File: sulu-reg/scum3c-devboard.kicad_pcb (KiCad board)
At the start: 2 copper layers, 41.7 x 36.1 mm, 55 parts, among them J1 Conn_02x11_Odd_Even, J10 through_hole, J11 through_hole, J12 through_hole, J13 through_hole, J14 through_hole, J15 through_hole, J16 through_hole, J17 through_hole, J18 through_hole, J19 through_hole, J2 Conn_02x10_Odd_Even, J20 through_hole, J21 through_hole, J3 Conn_02x05_Odd_Even, J4 73391-0060, J5 through_hole, J6 through_hole, J7 through_hole, J8 through_hole, J9 through_hole, U1 scum3, U2 S-85S1AB18-I6T1U, U3 S-85S1AB11-I6T1U, U9AB1 ICM-20948

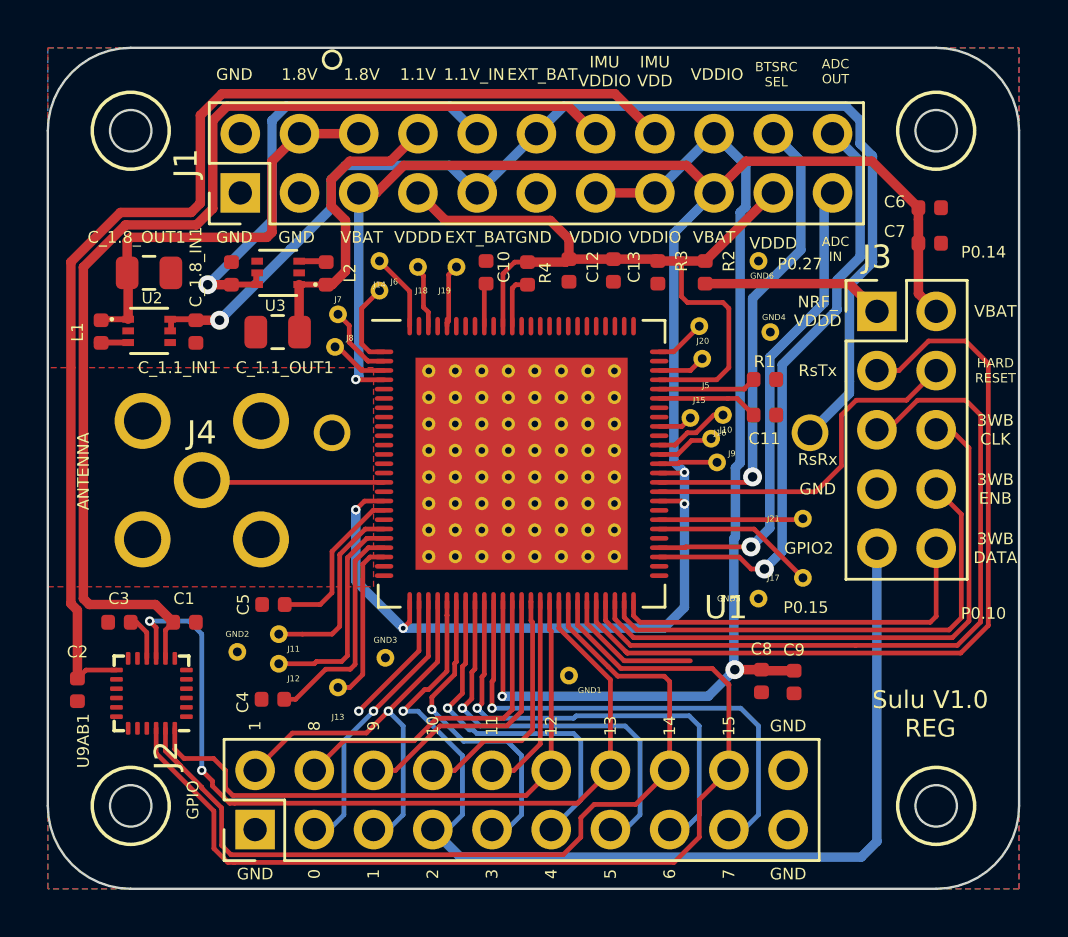
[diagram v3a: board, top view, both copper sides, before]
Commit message: added gnd connections to antenna
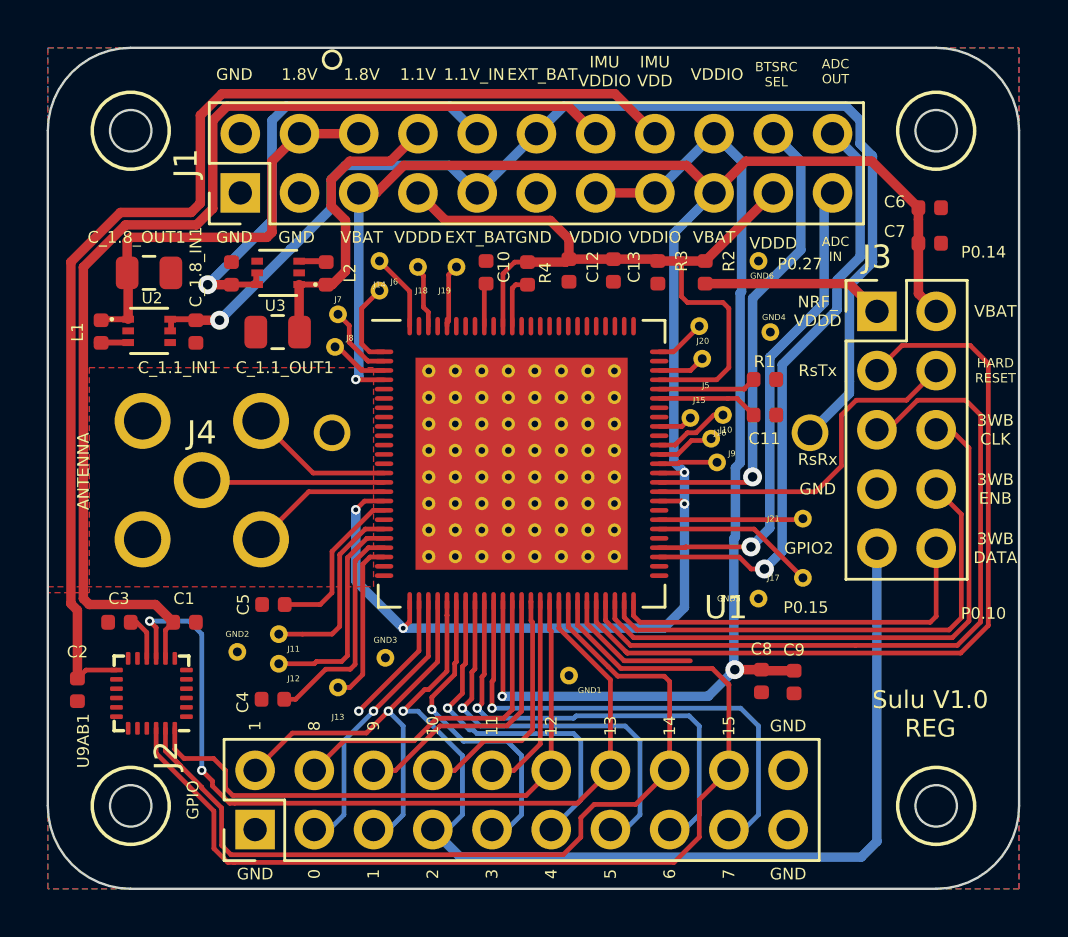
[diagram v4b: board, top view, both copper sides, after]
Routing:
- net GND: track 11.8 -> 24.2 mm
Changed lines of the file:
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@@
     (thickness 1.6)
     (drawings 783)
-    (tracks 508)
+    (tracks 511)
     (zones 0)
     (modules 55)
@@
   (layers
     (0 F.Cu mixed)
-    (31 B.Cu mixed hide)
+    (31 B.Cu mixed)
     (32 B.Adhes user)
     (33 F.Adhes user)
@@
     (pad_to_mask_clearance 0)
     (aux_axis_origin 0 0)
-    (grid_origin 121.285 75.565)
     (visible_elements 7FFFFFFF)
     (pcbplotparams
@@
   (segment (start 121.965 96.255) (end 121.965 98.38) (width 0.2032) (layer F.Cu) (net 1) (status 10))
   (segment (start 121.965 98.38) (end 119.38 100.965) (width 0.2032) (layer F.Cu) (net 1))
+  (segment (start 117.425 90.755) (end 115.189 88.519) (width 0.2032) (layer F.Cu) (net 1))
+  (segment (start 120.465 90.755) (end 117.425 90.755) (width 0.2032) (layer F.Cu) (net 1))
+  (segment (start 117.233 91.555) (end 120.465 91.555) (width 0.2032) (layer F.Cu) (net 1))
+  (segment (start 115.189 93.599) (end 117.233 91.555) (width 0.2032) (layer F.Cu) (net 1))
   (via (at 133.35 92.075) (size 0.4064) (drill 0.2032) (layers F.Cu B.Cu) (net 2))
   (segment (start 132.265 91.955) (end 133.23 91.955) (width 0.2032) (layer F.Cu) (net 2) (status 10))
@@
   (segment (start 134.366 100.33) (end 135.509 99.187) (width 0.4064) (layer B.Cu) (net 4))
   (segment (start 125.5332 100.33) (end 134.366 100.33) (width 0.4064) (layer B.Cu) (net 4))
-  (segment (start 135.979799 77.559799) (end 134.62 76.2) (width 0.4064) (layer B.Cu) (net 4))
-  (segment (start 135.979799 79.337799) (end 135.979799 77.559799) (width 0.4064) (layer B.Cu) (net 4))
-  (segment (start 135.73758 79.580018) (end 135.979799 79.337799) (width 0.4064) (layer B.Cu) (net 4))
-  (segment (start 135.73758 90.32242) (end 135.73758 79.580018) (width 0.4064) (layer B.Cu) (net 4))
   (segment (start 135.509 99.187) (end 135.466386 99.144386) (width 0.4064) (layer B.Cu) (net 4))
   (segment (start 135.534389 93.499441) (end 135.534389 90.525611) (width 0.4064) (layer B.Cu) (net 4))
@@
   (segment (start 135.466386 93.567444) (end 135.534389 93.499441) (width 0.4064) (layer B.Cu) (net 4))
   (segment (start 135.534389 90.525611) (end 135.73758 90.32242) (width 0.4064) (layer B.Cu) (net 4))
+  (segment (start 135.73758 83.038467) (end 135.73758 90.32242) (width 0.4064) (layer B.Cu) (net 4))
+  (segment (start 135.800201 82.975846) (end 135.73758 83.038467) (width 0.4064) (layer B.Cu) (net 4))
+  (segment (start 135.800201 77.380201) (end 135.800201 82.975846) (width 0.4064) (layer B.Cu) (net 4))
+  (segment (start 134.62 76.2) (end 135.800201 77.380201) (width 0.4064) (layer B.Cu) (net 4))
   (segment (start 135.607 87.555) (end 136.317 88.265) (width 0.2032) (layer F.Cu) (net 5))
   (segment (start 135.203 87.555) (end 135.607 87.555) (width 0.2032) (layer F.Cu) (net 5))
@@
   (segment (start 130.828526 98.406474) (end 130.897893 98.47584) (width 0.2032) (layer F.Cu) (net 18))
   (segment (start 129.565 97.142947) (end 130.828526 98.406474) (width 0.2032) (layer F.Cu) (net 18))
-  (segment (start 142.54867 86.36) (end 141.605 86.36) (width 0.2032) (layer F.Cu) (net 18))
-  (segment (start 143.81867 85.09) (end 142.54867 86.36) (width 0.2032) (layer F.Cu) (net 18))
-  (segment (start 145.415 85.09) (end 143.81867 85.09) (width 0.2032) (layer F.Cu) (net 18))
   (segment (start 130.828526 98.406474) (end 130.897892 98.47584) (width 0.2032) (layer F.Cu) (net 18))
-  (segment (start 146.38021 86.05521) (end 145.415 85.09) (width 0.2032) (layer F.Cu) (net 18))
   (segment (start 130.897892 98.47584) (end 145.196146 98.47584) (width 0.2032) (layer F.Cu) (net 18))
   (segment (start 145.196146 98.47584) (end 146.38021 97.291777) (width 0.2032) (layer F.Cu) (net 18))
   (segment (start 146.38021 97.291777) (end 146.38021 86.05521) (width 0.2032) (layer F.Cu) (net 18))
+  (segment (start 145.606399 85.281399) (end 146.38021 86.05521) (width 0.2032) (layer F.Cu) (net 18))
+  (segment (start 142.683601 85.281399) (end 145.606399 85.281399) (width 0.2032) (layer F.Cu) (net 18))
+  (segment (start 141.605 86.36) (end 142.683601 85.281399) (width 0.2032) (layer F.Cu) (net 18))
   (segment (start 142.071986 88.9) (end 141.605 88.9) (width 0.2032) (layer F.Cu) (net 19) (status 30))
   (segment (start 143.341986 87.63) (end 142.071986 88.9) (width 0.2032) (layer F.Cu) (net 19) (status 20))
@@
       (pts
         (xy 147.701 108.585) (xy 106.045 108.585) (xy 106.045 95.631) (xy 120.015 95.631) (xy 120.015 86.233)
-        (xy 106.045 86.233) (xy 106.045 72.517) (xy 147.701 72.517)
+        (xy 107.823 86.233) (xy 107.823 95.885) (xy 106.045 95.885) (xy 106.045 72.517) (xy 147.701 72.517)
       )
     )

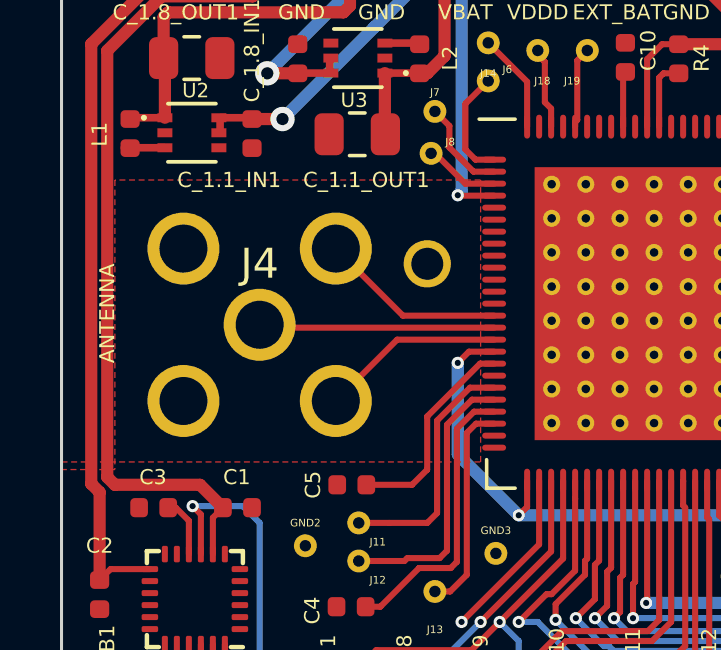
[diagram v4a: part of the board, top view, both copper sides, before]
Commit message: put ground on west of antenna
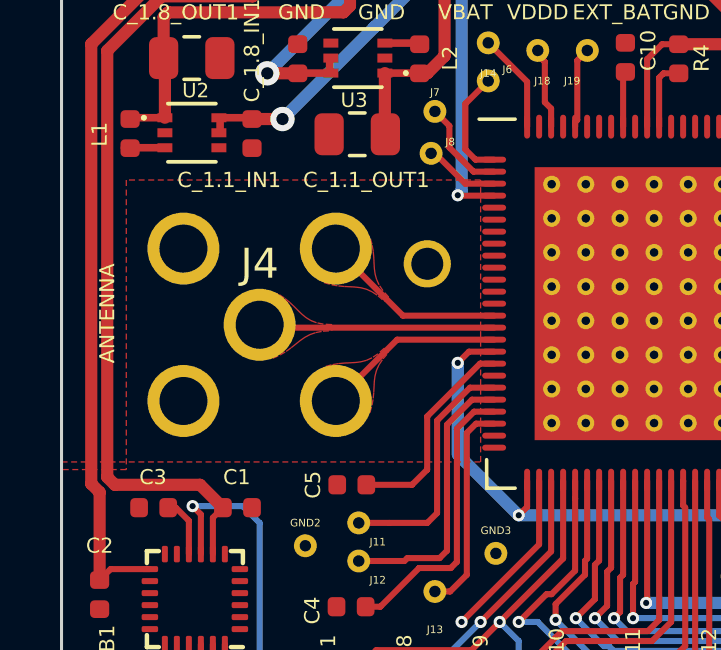
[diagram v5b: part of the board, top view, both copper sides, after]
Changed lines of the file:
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@@
       (pts
         (xy 147.701 108.585) (xy 106.045 108.585) (xy 106.045 95.631) (xy 120.015 95.631) (xy 120.015 86.233)
-        (xy 107.823 86.233) (xy 107.823 95.885) (xy 106.045 95.885) (xy 106.045 72.517) (xy 147.701 72.517)
+        (xy 108.204 86.233) (xy 108.204 95.885) (xy 106.045 95.885) (xy 106.045 72.517) (xy 147.701 72.517)
       )
     )
@@
       )
     )
+  )
+  (zone (net 63) (net_name /scumsheet/ANTENNA) (layer F.Cu) (hatch edge 0.508)
+    (priority 16962)
+    (connect_pads yes (clearance 0.127))
+    (min_thickness 0.0254)
+    (fill yes (arc_segments 32) (thermal_gap 0.508) (thermal_bridge_width 0.508))
+    (polygon
+      (pts
+        (xy 115.055 91.0534) (xy 114.774304 91.037184) (xy 114.546409 90.991167) (xy 114.359914 90.919298) (xy 114.203421 90.825523)
+        (xy 114.065529 90.71379) (xy 113.93484 90.588046) (xy 113.799954 90.452239) (xy 113.649471 90.310316) (xy 113.471992 90.166224)
+        (xy 113.256117 90.023912) (xy 112.050892 91.01139) (xy 113.084719 92.1771) (xy 113.329824 92.065867) (xy 113.531784 91.946321)
+        (xy 113.702772 91.823179) (xy 113.85496 91.701157) (xy 114.000523 91.584969) (xy 114.151632 91.479331) (xy 114.320461 91.388959)
+        (xy 114.519183 91.31857) (xy 114.759972 91.272878) (xy 115.055 91.2566)
+      )
+    )
+  )
+  (zone (net 1) (net_name GND) (layer F.Cu) (hatch edge 0.508)
+    (priority 16962)
+    (connect_pads yes (clearance 0.127))
+    (min_thickness 0.0254)
+    (fill yes (arc_segments 32) (thermal_gap 0.508) (thermal_bridge_width 0.508))
+    (polygon
+      (pts
+        (xy 116.950827 90.137143) (xy 116.760467 89.923664) (xy 116.628899 89.726868) (xy 116.544705 89.54152) (xy 116.496464 89.362391)
+        (xy 116.472757 89.184247) (xy 116.462164 89.001856) (xy 116.453265 88.809987) (xy 116.434642 88.603407) (xy 116.394873 88.376886)
+        (xy 116.32254 88.12519) (xy 114.764736 88.094736) (xy 114.79519 89.65254) (xy 115.046886 89.724873) (xy 115.273407 89.764642)
+        (xy 115.479987 89.783265) (xy 115.671856 89.792164) (xy 115.854247 89.802757) (xy 116.032391 89.826464) (xy 116.21152 89.874705)
+        (xy 116.396868 89.958899) (xy 116.593664 90.090467) (xy 116.807143 90.280827)
+      )
+    )
+  )
+  (zone (net 1) (net_name GND) (layer F.Cu) (hatch edge 0.508)
+    (priority 16962)
+    (connect_pads yes (clearance 0.127))
+    (min_thickness 0.0254)
+    (fill yes (arc_segments 32) (thermal_gap 0.508) (thermal_bridge_width 0.508))
+    (polygon
+      (pts
+        (xy 116.807143 91.837173) (xy 116.593664 92.027532) (xy 116.396868 92.1591) (xy 116.21152 92.243294) (xy 116.032391 92.291535)
+        (xy 115.854247 92.315242) (xy 115.671856 92.325835) (xy 115.479987 92.334734) (xy 115.273407 92.353357) (xy 115.046886 92.393126)
+        (xy 114.79519 92.46546) (xy 114.764736 94.023264) (xy 116.32254 93.99281) (xy 116.394873 93.741113) (xy 116.434642 93.514592)
+        (xy 116.453265 93.308012) (xy 116.462164 93.116143) (xy 116.472757 92.933752) (xy 116.496464 92.755608) (xy 116.544705 92.576479)
+        (xy 116.628899 92.391131) (xy 116.760467 92.194335) (xy 116.950827 91.980857)
+      )
+    )

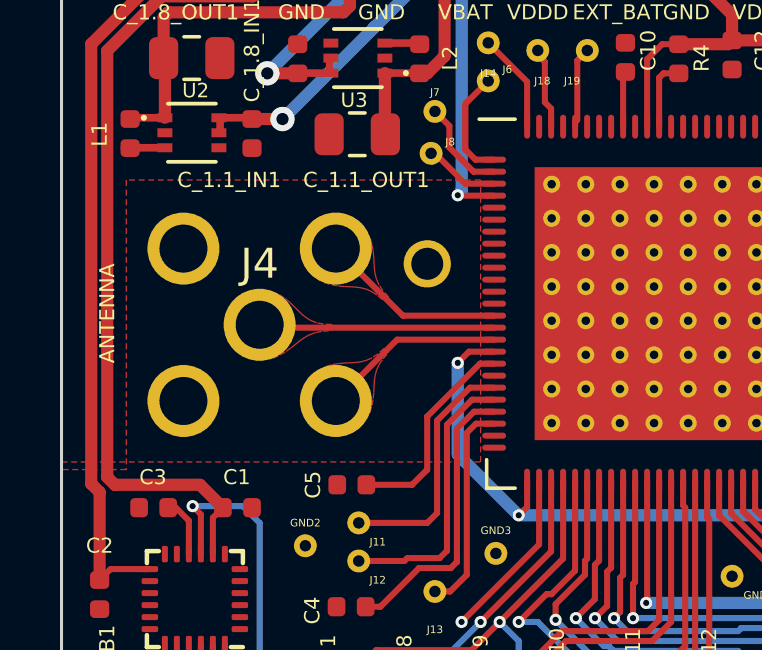
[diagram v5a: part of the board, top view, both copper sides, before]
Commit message: shifted antenna south to match ldo board
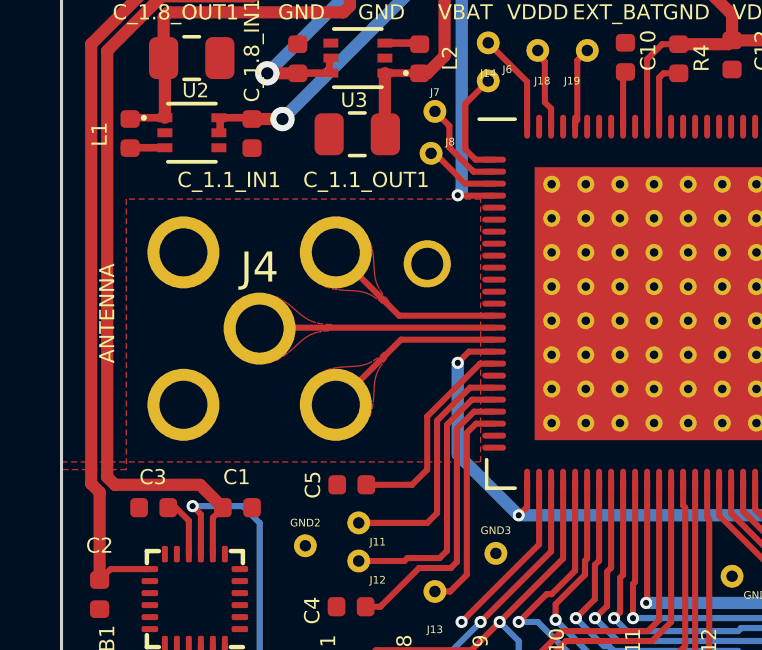
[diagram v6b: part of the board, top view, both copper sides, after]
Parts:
- moved J4 0.13 mm to (112.6, 91.2)
